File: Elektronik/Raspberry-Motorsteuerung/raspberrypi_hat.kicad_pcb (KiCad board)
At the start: 2 copper layers, 65 x 56 mm, 31 parts, among them J1 Barrel_Jack_Switch, J10 Conn_01x02_Male, J11 Conn_01x02_Male, J15 Conn_01x02_Male, J2 Conn_01x04_Male, J3 40HAT, J6 Conn_01x04_Male, J8 Conn_01x02_Male, J9 CONN_01X02, Q1 DMG2305UX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

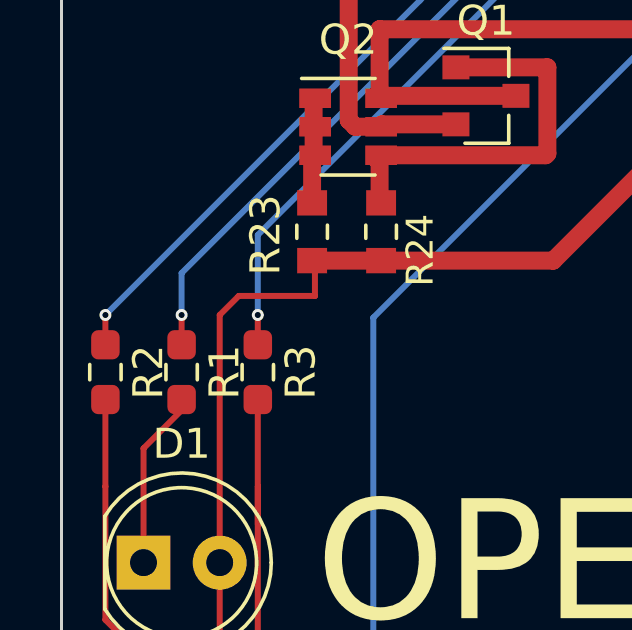
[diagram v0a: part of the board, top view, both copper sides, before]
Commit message: increased via size to 0.6/0.3mm
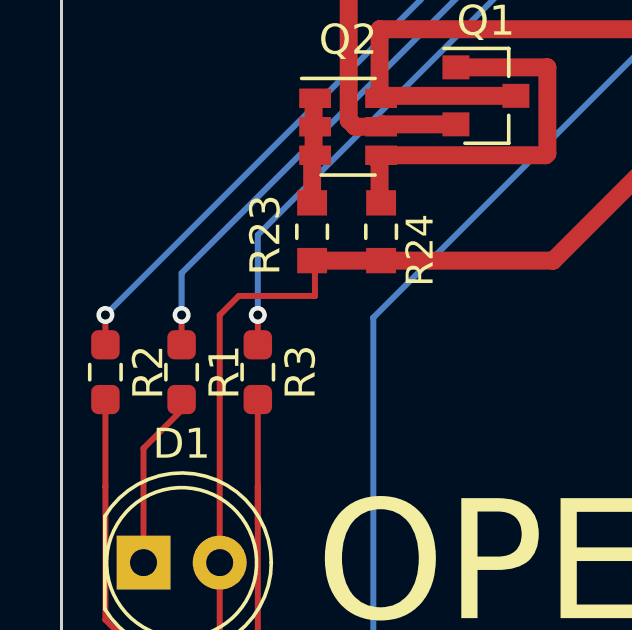
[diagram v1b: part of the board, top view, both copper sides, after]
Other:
- net class Default: via_dia 0.4 -> 0.6; via_drill 0.2 -> 0.3

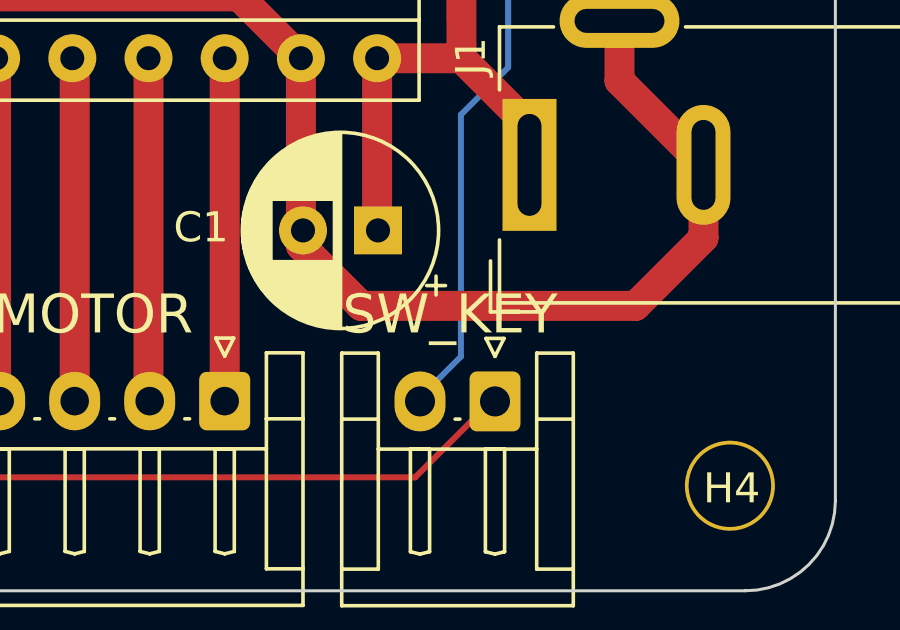
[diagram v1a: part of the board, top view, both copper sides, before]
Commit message: fixed second SW_KEY to SW_WIN in silkscreen
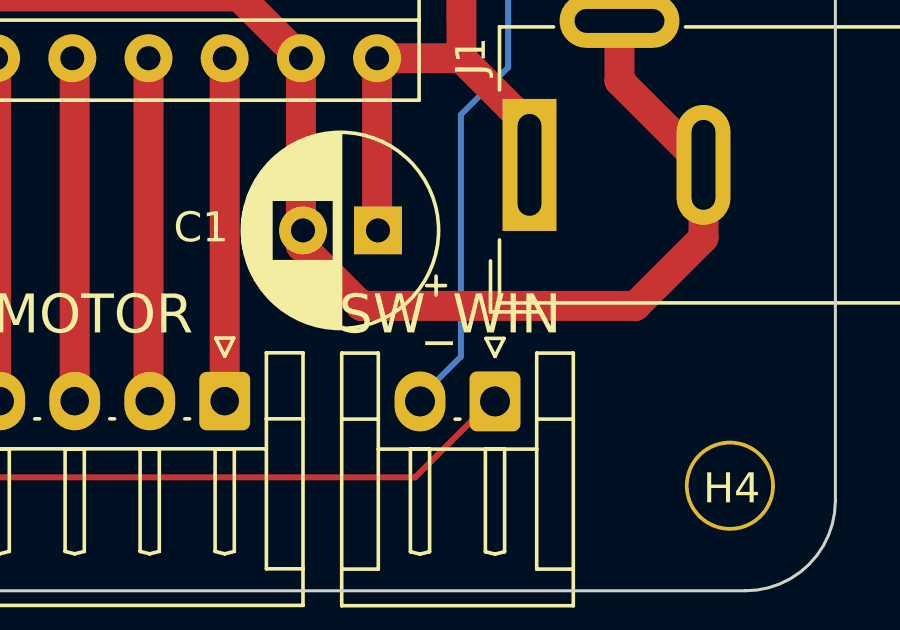
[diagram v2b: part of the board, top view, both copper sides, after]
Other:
- board text added: "SW_WIN"

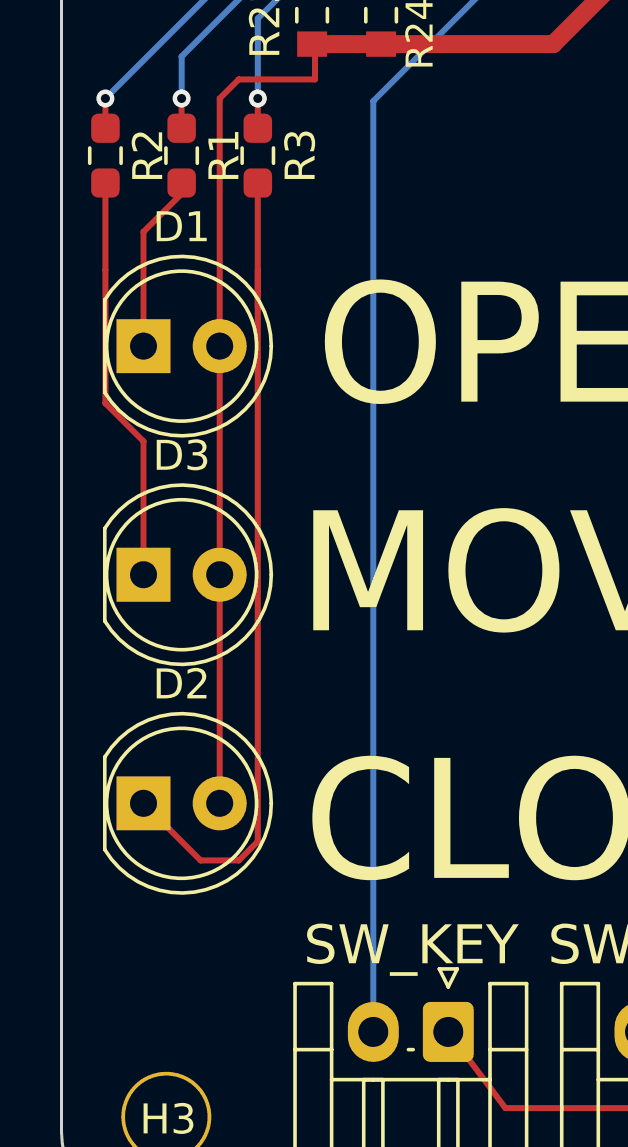
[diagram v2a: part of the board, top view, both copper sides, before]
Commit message: fixed LED orientation, C1 symbol, added 'rev 2' label, did not export gerber files
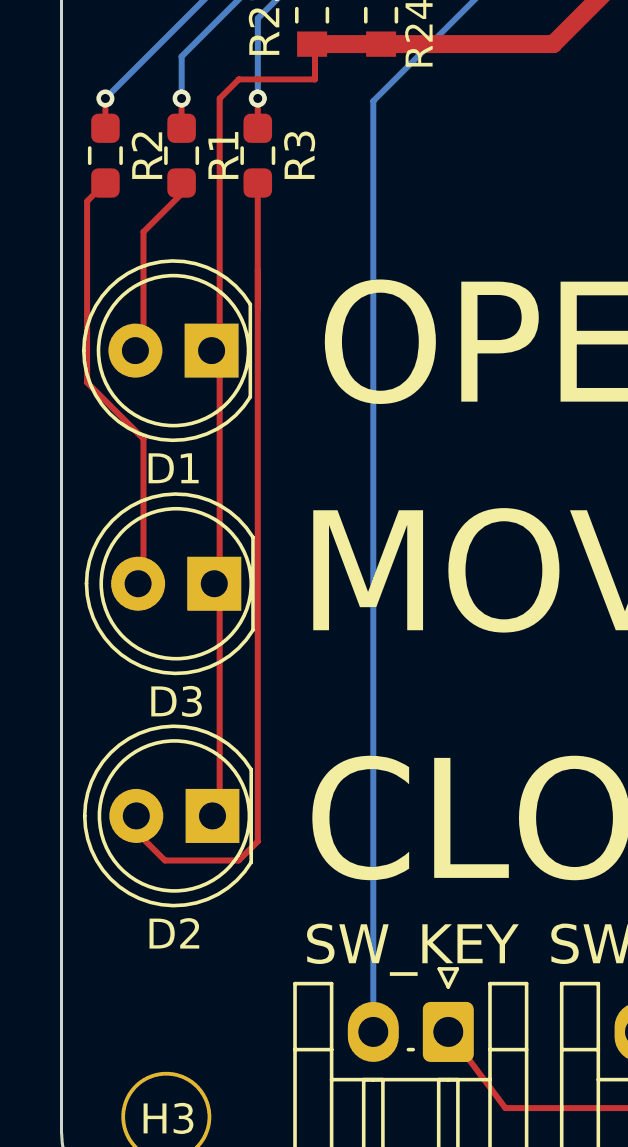
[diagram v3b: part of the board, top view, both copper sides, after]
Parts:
- moved D3 2.38 mm to (83.6, 95.5), turned to 180 degrees
- moved D2 2.34 mm to (83.6, 103.3), turned to 180 degrees
- moved D1 2.27 mm to (83.5, 87.8), turned to 180 degrees
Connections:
- D1 pad 1: Net-(D1-Pad1) -> GND
- D1 pad 2: GND -> Net-(D1-Pad2)
- D2 pad 1: Net-(D2-Pad1) -> GND
- D2 pad 2: GND -> Net-(D2-Pad2)
- D3 pad 1: Net-(D3-Pad1) -> GND
- D3 pad 2: GND -> Net-(D3-Pad2)
- R1 pad 2: Net-(D1-Pad1) -> Net-(D1-Pad2)
- R2 pad 2: Net-(D3-Pad1) -> Net-(D3-Pad2)
- R3 pad 2: Net-(D2-Pad1) -> Net-(D2-Pad2)
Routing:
- net Net-(D2-Pad2): track 0.00 -> 28.5 mm
- net Net-(D2-Pad1): track 28.1 -> 0.00 mm
- net Net-(D3-Pad2): track 0.00 -> 14.1 mm
- net Net-(D3-Pad1): track 13.6 -> 0.00 mm
- net Net-(D1-Pad2): track 0.00 -> 5.96 mm
- net Net-(D1-Pad1): track 5.96 -> 0.00 mm
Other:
- board text added: "rev 2"
